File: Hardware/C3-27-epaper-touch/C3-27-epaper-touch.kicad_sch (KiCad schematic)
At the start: 64 parts, among them J1 AFC24-S24FIC-00, J2 USB_C_Programming, J3 Conn_01x06, J4 Conn_01x06_Female, J5 Groove sensor, Q1 Si1308, Q2 BC817, Q3 BC817, U1 ESP32-C3-WROOM-02-N4, U2 CP2102N-A02-GQFN28R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

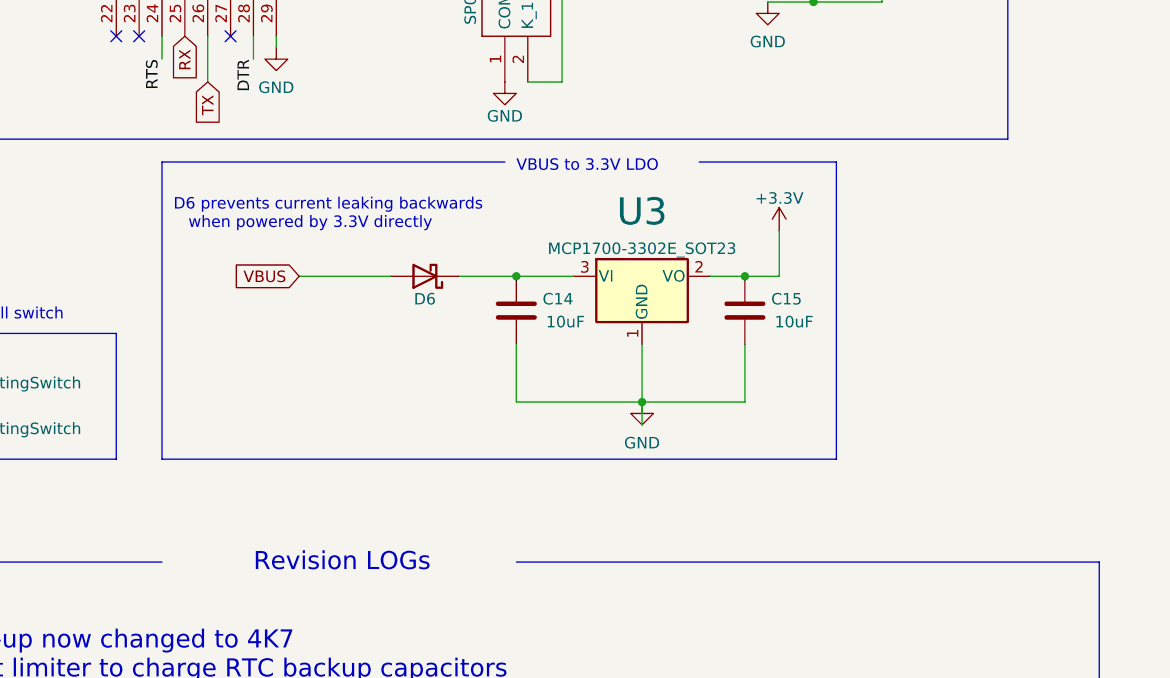
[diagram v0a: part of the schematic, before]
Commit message: Switch LDO to RT9013-33GB Ref https://github.com/martinberlin/H-spi-adapters/issues/9
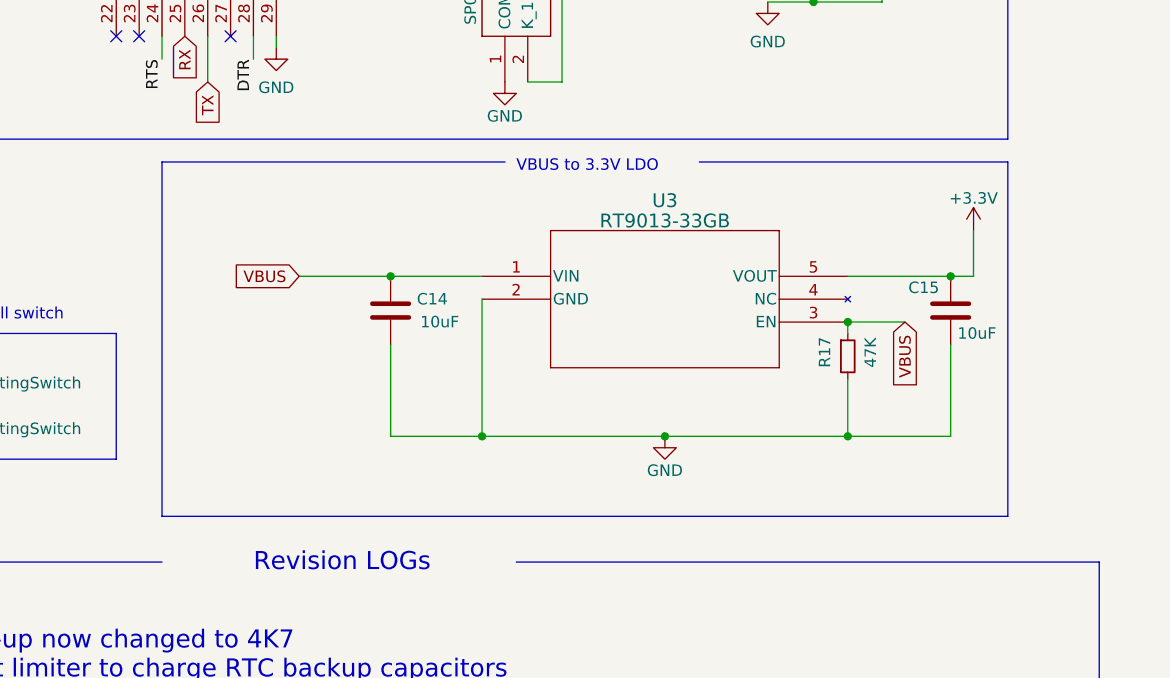
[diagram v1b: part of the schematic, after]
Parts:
- removed D6: 1N5819WS, Diode_SMD:D_SOD-323, symbol Diode:MBR0530
- removed U3: MCP1700-3302E_SOT23, Package_TO_SOT_SMD:SOT-23, symbol Regulator_Linear:MCP1700-3302E_SOT23
- added R17: 47K, Resistor_SMD:R_0603_1608Metric, symbol Device:R_Small
- added U3: RT9013-33GB, footprint:RT9013-33GB, symbol LDO:RT9013-33GB
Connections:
- net +3V3: now also U3.5 (VOUT)
- net +5V: now also C14.1, R17.1, U3.1 (VIN), U3.3 (EN)
- net GND: now also R17.2, U3.2 (GND)
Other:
- note removed: "D6 prevents current leaking backwards when powered by 3.3V directly"
- moved on the sheet: C14, C15
